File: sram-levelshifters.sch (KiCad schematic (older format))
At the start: 25 parts, among them U10 TXB0108-PW, U11 ISSI61WV5128BL, U12 ISSI61WV5128BL, U13 ISSI61WV5128BL, U14 ISSI61WV5128BL, U4 TXB0108-PW, U5 TXB0108-PW, U6 TXB0108-PW, U7 74HC04, U8 TXB0108-PW, U9 74LS32

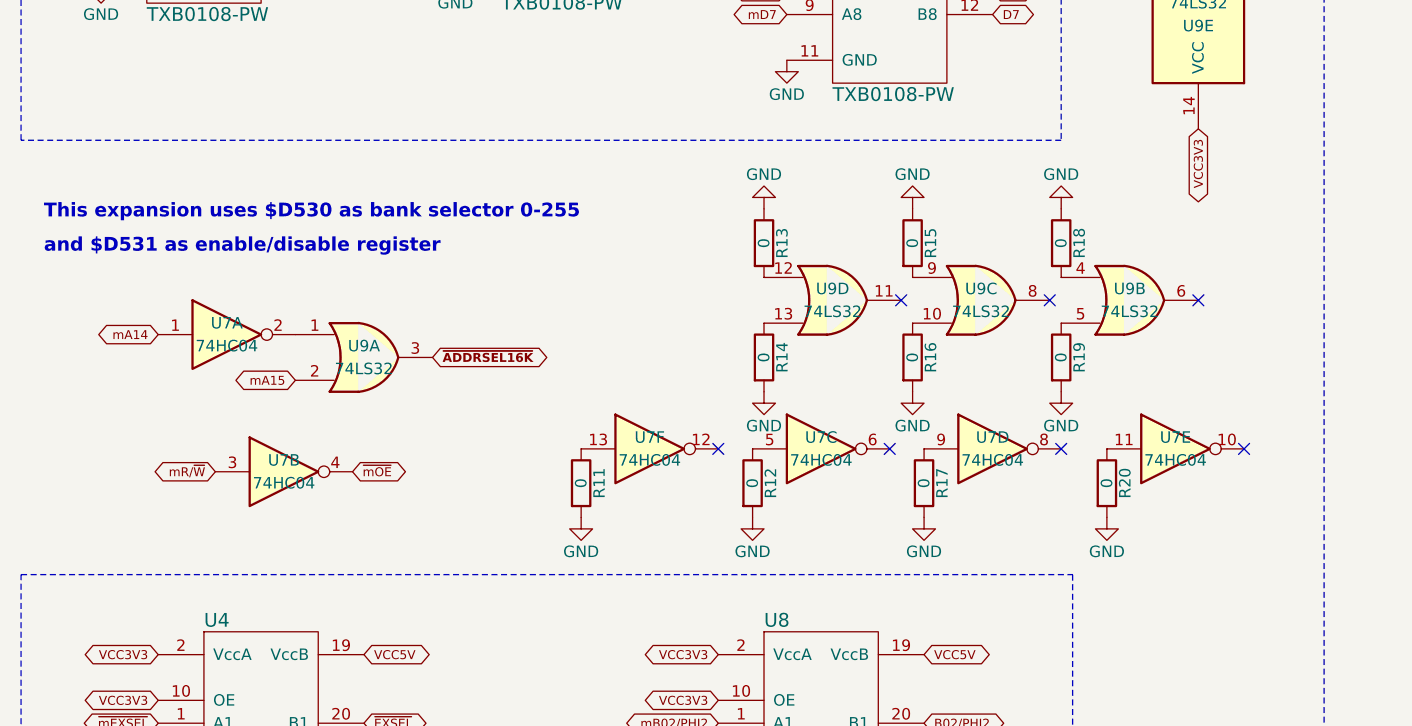
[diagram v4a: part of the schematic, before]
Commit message: Added D3xx selection logic for PIA (6520) if needed
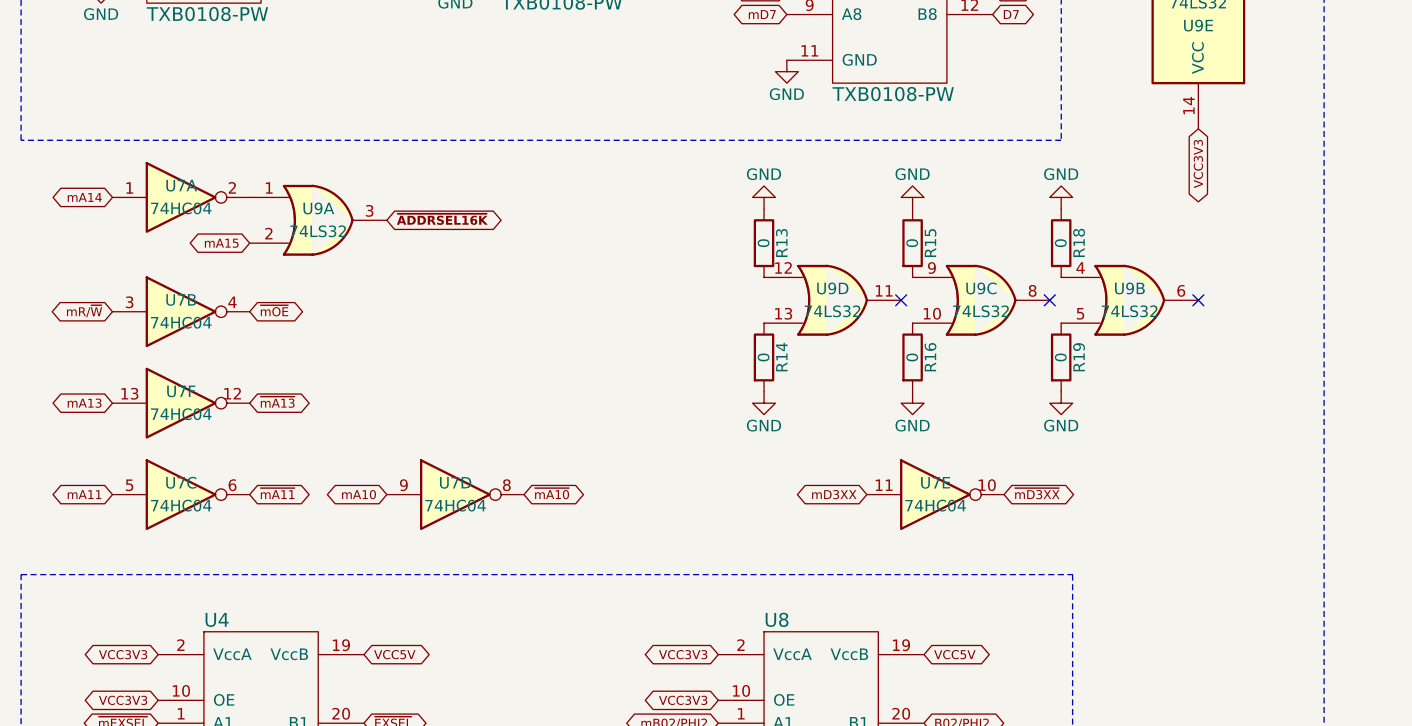
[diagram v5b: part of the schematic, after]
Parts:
- removed R11, R12, R17, R20: 0, Resistors_SMD:R_1206_HandSoldering, symbol R
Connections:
- net mA10: now also U7.9
- net mA11: now also U7.5
- net mA13: now also U7.13
- net ~mA11: now reaches U7.6
- net ~mA10: now reaches U7.8
- net ~mD3XX: now reaches U7.10
- net mD3XX: now reaches U7.11
- net ~mA13: now reaches U7.12
- no-connect marks 11 -> 7
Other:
- note removed: "This expansion uses $D530 as bank selector 0-255"
- note removed: "and $D531 as enable/disable register"
- moved on the sheet: U7A, U7B, U7C, U7D, U7E, U7F, U9A
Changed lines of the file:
@@
 Text Notes 6450 800  0    59   ~ 12
 STATIC RAM
-Text GLabel 2400 3900 2    39   BiDi ~ 8
+Text GLabel 2200 3300 2    39   BiDi ~ 8
 ~ADDRSEL16K
 $Comp
 L 74LS32 U9
 U 1 1 5C2DFACA
-P 2100 3900
-F 0 "U9" H 2100 3950 50  0000 C CNN
-F 1 "74LS32" H 2100 3850 50  0000 C CNN
-F 2 "Housings_SSOP:SSOP-14_5.3x6.2mm_Pitch0.65mm" H 2100 3900 50  0001 C CNN
-F 3 "" H 2100 3900 60  0001 C CNN
-	1    2100 3900
+P 1900 3300
+F 0 "U9" H 1900 3350 50  0000 C CNN
+F 1 "74LS32" H 1900 3250 50  0000 C CNN
+F 2 "Housings_SSOP:SSOP-14_5.3x6.2mm_Pitch0.65mm" H 1900 3300 50  0001 C CNN
+F 3 "" H 1900 3300 60  0001 C CNN
+	1    1900 3300
 	1    0    0    -1
 $EndComp
@@
 NoConn ~ 5100 3650
 NoConn ~ 4450 3650
-Text GLabel 1800 4000 0    39   BiDi ~ 0
+Text GLabel 1600 3400 0    39   BiDi ~ 0
 mA15
-Text GLabel 1200 3800 0    39   BiDi ~ 0
+Text GLabel 1000 3200 0    39   BiDi ~ 0
 mA14
 $Comp
 L 74HC04 U7
 U 1 1 5C2DFE46
-P 1500 3800
-F 0 "U7" H 1500 3850 50  0000 C CNN
-F 1 "74HC04" H 1500 3750 50  0000 C CNN
-F 2 "Housings_SSOP:TSSOP-14_4.4x5mm_Pitch0.65mm" H 1500 3800 50  0001 C CNN
-F 3 "" H 1500 3800 60  0001 C CNN
-	1    1500 3800
+P 1300 3200
+F 0 "U7" H 1300 3250 50  0000 C CNN
+F 1 "74HC04" H 1300 3150 50  0000 C CNN
+F 2 "Housings_SSOP:TSSOP-14_4.4x5mm_Pitch0.65mm" H 1300 3200 50  0001 C CNN
+F 3 "" H 1300 3200 60  0001 C CNN
+	1    1300 3200
 	1    0    0    -1
 $EndComp
@@
 L 74HC04 U7
 U 2 1 5C2DFEE1
-P 1750 4400
-F 0 "U7" H 1750 4450 50  0000 C CNN
-F 1 "74HC04" H 1750 4350 50  0000 C CNN
-F 2 "Housings_SSOP:TSSOP-14_4.4x5mm_Pitch0.65mm" H 1750 4400 50  0001 C CNN
-F 3 "" H 1750 4400 60  0001 C CNN
-	2    1750 4400
+P 1300 3700
+F 0 "U7" H 1300 3750 50  0000 C CNN
+F 1 "74HC04" H 1300 3650 50  0000 C CNN
+F 2 "Housings_SSOP:TSSOP-14_4.4x5mm_Pitch0.65mm" H 1300 3700 50  0001 C CNN
+F 3 "" H 1300 3700 60  0001 C CNN
+	2    1300 3700
 	1    0    0    -1
 $EndComp
@@
 L 74HC04 U7
 U 3 1 5C2DFF28
-P 4100 4300
-F 0 "U7" H 4100 4350 50  0000 C CNN
-F 1 "74HC04" H 4100 4250 50  0000 C CNN
-F 2 "Housings_SSOP:TSSOP-14_4.4x5mm_Pitch0.65mm" H 4100 4300 50  0001 C CNN
-F 3 "" H 4100 4300 60  0001 C CNN
-	3    4100 4300
+P 1300 4500
+F 0 "U7" H 1300 4550 50  0000 C CNN
+F 1 "74HC04" H 1300 4450 50  0000 C CNN
+F 2 "Housings_SSOP:TSSOP-14_4.4x5mm_Pitch0.65mm" H 1300 4500 50  0001 C CNN
+F 3 "" H 1300 4500 60  0001 C CNN
+	3    1300 4500
 	1    0    0    -1
 $EndComp
@@
 L 74HC04 U7
 U 4 1 5C2E0001
-P 4850 4300
-F 0 "U7" H 4850 4350 50  0000 C CNN
-F 1 "74HC04" H 4850 4250 50  0000 C CNN
-F 2 "Housings_SSOP:TSSOP-14_4.4x5mm_Pitch0.65mm" H 4850 4300 50  0001 C CNN
-F 3 "" H 4850 4300 60  0001 C CNN
-	4    4850 4300
+P 2500 4500
+F 0 "U7" H 2500 4550 50  0000 C CNN
+F 1 "74HC04" H 2500 4450 50  0000 C CNN
+F 2 "Housings_SSOP:TSSOP-14_4.4x5mm_Pitch0.65mm" H 2500 4500 50  0001 C CNN
+F 3 "" H 2500 4500 60  0001 C CNN
+	4    2500 4500
 	1    0    0    -1
 $EndComp
@@
 L 74HC04 U7
 U 5 1 5C2E0114
-P 5650 4300
-F 0 "U7" H 5650 4350 50  0000 C CNN
-F 1 "74HC04" H 5650 4250 50  0000 C CNN
-F 2 "Housings_SSOP:TSSOP-14_4.4x5mm_Pitch0.65mm" H 5650 4300 50  0001 C CNN
-F 3 "" H 5650 4300 60  0001 C CNN
-	5    5650 4300
+P 4600 4500
+F 0 "U7" H 4600 4550 50  0000 C CNN
+F 1 "74HC04" H 4600 4450 50  0000 C CNN
+F 2 "Housings_SSOP:TSSOP-14_4.4x5mm_Pitch0.65mm" H 4600 4500 50  0001 C CNN
+F 3 "" H 4600 4500 60  0001 C CNN
+	5    4600 4500
 	1    0    0    -1
 $EndComp
@@
 L 74HC04 U7
 U 6 1 5C2E0161
-P 3350 4300
-F 0 "U7" H 3350 4350 50  0000 C CNN
-F 1 "74HC04" H 3350 4250 50  0000 C CNN
-F 2 "Housings_SSOP:TSSOP-14_4.4x5mm_Pitch0.65mm" H 3350 4300 50  0001 C CNN
-F 3 "" H 3350 4300 60  0001 C CNN
-	6    3350 4300
+P 1300 4100
+F 0 "U7" H 1300 4150 50  0000 C CNN
+F 1 "74HC04" H 1300 4050 50  0000 C CNN
+F 2 "Housings_SSOP:TSSOP-14_4.4x5mm_Pitch0.65mm" H 1300 4100 50  0001 C CNN
+F 3 "" H 1300 4100 60  0001 C CNN
+	6    1300 4100
 	1    0    0    -1
 $EndComp
@@
 Text GLabel 7150 6050 0    39   BiDi ~ 0
 PB4
-Text GLabel 1450 4400 0    39   BiDi ~ 0
+Text GLabel 1000 3700 0    39   BiDi ~ 0
 mR/~W
-Text GLabel 2050 4400 2    39   BiDi ~ 0
+Text GLabel 1600 3700 2    39   BiDi ~ 0
 ~mOE
 Text GLabel 8350 2650 3    39   BiDi ~ 0
@@
 Text GLabel 8350 5550 3    39   BiDi ~ 0
 ~mOE
-Text Notes 700  3300 0    60   ~ 12
-This expansion uses $D530 as bank selector 0-255
-Text Notes 700  3450 0    60   ~ 12
-and $D531 as enable/disable register
 Text GLabel 4550 5700 2    39   BiDi ~ 0
 ~S4
@@
 Text GLabel 3650 5700 0    39   BiDi ~ 0
 ~mS4
-NoConn ~ 3650 4300
-NoConn ~ 4400 4300
-NoConn ~ 5150 4300
-NoConn ~ 5950 4300
-$Comp
-L GND #PWR041
-U 1 1 5C371152
-P 5350 4600
-F 0 "#PWR041" H 5350 4350 50  0001 C CNN
-F 1 "GND" H 5350 4450 50  0000 C CNN
-F 2 "" H 5350 4600 50  0001 C CNN
-F 3 "" H 5350 4600 50  0001 C CNN
-	1    5350 4600
-	1    0    0    -1
-$EndComp
-$Comp
-L R R20
-U 1 1 5C371196
-P 5350 4450
-F 0 "R20" V 5430 4450 50  0000 C CNN
-F 1 "0" V 5350 4450 50  0000 C CNN
-F 2 "Resistors_SMD:R_1206_HandSoldering" V 5280 4450 50  0001 C CNN
-F 3 "" H 5350 4450 50  0000 C CNN
-	1    5350 4450
-	1    0    0    -1
-$EndComp
-$Comp
-L R R17
-U 1 1 5C37121E
-P 4550 4450
-F 0 "R17" V 4630 4450 50  0000 C CNN
-F 1 "0" V 4550 4450 50  0000 C CNN
-F 2 "Resistors_SMD:R_1206_HandSoldering" V 4480 4450 50  0001 C CNN
-F 3 "" H 4550 4450 50  0000 C CNN
-	1    4550 4450
-	1    0    0    -1
-$EndComp
-$Comp
-L R R12
-U 1 1 5C371304
-P 3800 4450
-F 0 "R12" V 3880 4450 50  0000 C CNN
-F 1 "0" V 3800 4450 50  0000 C CNN
-F 2 "Resistors_SMD:R_1206_HandSoldering" V 3730 4450 50  0001 C CNN
-F 3 "" H 3800 4450 50  0000 C CNN
-	1    3800 4450
-	1    0    0    -1
-$EndComp
-$Comp
-L R R11
-U 1 1 5C3713A0
-P 3050 4450
-F 0 "R11" V 3130 4450 50  0000 C CNN
-F 1 "0" V 3050 4450 50  0000 C CNN
-F 2 "Resistors_SMD:R_1206_HandSoldering" V 2980 4450 50  0001 C CNN
-F 3 "" H 3050 4450 50  0000 C CNN
-	1    3050 4450
-	1    0    0    -1
-$EndComp
-$Comp
-L GND #PWR042
-U 1 1 5C37141A
-P 4550 4600
-F 0 "#PWR042" H 4550 4350 50  0001 C CNN
-F 1 "GND" H 4550 4450 50  0000 C CNN
-F 2 "" H 4550 4600 50  0001 C CNN
-F 3 "" H 4550 4600 50  0001 C CNN
-	1    4550 4600
-	1    0    0    -1
-$EndComp
-$Comp
-L GND #PWR043
-U 1 1 5C371479
-P 3800 4600
-F 0 "#PWR043" H 3800 4350 50  0001 C CNN
-F 1 "GND" H 3800 4450 50  0000 C CNN
-F 2 "" H 3800 4600 50  0001 C CNN
-F 3 "" H 3800 4600 50  0001 C CNN
-	1    3800 4600
-	1    0    0    -1
-$EndComp
-$Comp
-L GND #PWR044
-U 1 1 5C3714D8
-P 3050 4600
-F 0 "#PWR044" H 3050 4350 50  0001 C CNN
-F 1 "GND" H 3050 4450 50  0000 C CNN
-F 2 "" H 3050 4600 50  0001 C CNN
-F 3 "" H 3050 4600 50  0001 C CNN
-	1    3050 4600
-	1    0    0    -1
-$EndComp
 $Comp
 L R R14
@@
 $EndComp
 $Comp
-L GND #PWR045
+L GND #PWR041
 U 1 1 5C371981
 P 5150 3250
-F 0 "#PWR045" H 5150 3000 50  0001 C CNN
+F 0 "#PWR041" H 5150 3000 50  0001 C CNN
 F 1 "GND" H 5150 3100 50  0000 C CNN
 F 2 "" H 5150 3250 50  0001 C CNN
@@
 $EndComp
 $Comp
-L GND #PWR046
+L GND #PWR042
 U 1 1 5C3719F2
 P 4500 3250
-F 0 "#PWR046" H 4500 3000 50  0001 C CNN
+F 0 "#PWR042" H 4500 3000 50  0001 C CNN
 F 1 "GND" H 4500 3100 50  0000 C CNN
 F 2 "" H 4500 3250 50  0001 C CNN
@@
 $EndComp
 $Comp
-L GND #PWR047
+L GND #PWR043
 U 1 1 5C371A63
 P 3850 3250
-F 0 "#PWR047" H 3850 3000 50  0001 C CNN
+F 0 "#PWR043" H 3850 3000 50  0001 C CNN
 F 1 "GND" H 3850 3100 50  0000 C CNN
 F 2 "" H 3850 3250 50  0001 C CNN
@@
 $EndComp
 $Comp
-L GND #PWR048
+L GND #PWR044
 U 1 1 5C371AD4
 P 3850 4050
-F 0 "#PWR048" H 3850 3800 50  0001 C CNN
+F 0 "#PWR044" H 3850 3800 50  0001 C CNN
 F 1 "GND" H 3850 3900 50  0000 C CNN
 F 2 "" H 3850 4050 50  0001 C CNN
@@
 $EndComp
 $Comp
-L GND #PWR049
+L GND #PWR045
 U 1 1 5C371B45
 P 4500 4050
-F 0 "#PWR049" H 4500 3800 50  0001 C CNN
+F 0 "#PWR045" H 4500 3800 50  0001 C CNN
 F 1 "GND" H 4500 3900 50  0000 C CNN
 F 2 "" H 4500 4050 50  0001 C CNN
@@
 $EndComp
 $Comp
-L GND #PWR050
+L GND #PWR046
 U 1 1 5C371BB6
 P 5150 4050
-F 0 "#PWR050" H 5150 3800 50  0001 C CNN
+F 0 "#PWR046" H 5150 3800 50  0001 C CNN
 F 1 "GND" H 5150 3900 50  0000 C CNN
 F 2 "" H 5150 4050 50  0001 C CNN
@@
 VCC5V
 $Comp
-L GND #PWR051
+L GND #PWR047
 U 1 1 5C374058
 P 2500 2200
-F 0 "#PWR051" H 2500 1950 50  0001 C CNN
+F 0 "#PWR047" H 2500 1950 50  0001 C CNN
 F 1 "GND" H 2500 2050 50  0000 C CNN
 F 2 "" H 2500 2200 60  0001 C CNN
@@
 NoConn ~ 3650 6200
 NoConn ~ 3650 6100
+Text GLabel 1000 4100 0    39   BiDi ~ 0
+mA13
+Text GLabel 1600 4100 2    39   BiDi ~ 0
+~mA13
+Text GLabel 1000 4500 0    39   BiDi ~ 0
+mA11
+Text GLabel 1600 4500 2    39   BiDi ~ 0
+~mA11
+Text GLabel 2200 4500 0    39   BiDi ~ 0
+mA10
+Text GLabel 2800 4500 2    39   BiDi ~ 0
+~mA10
+Text GLabel 4300 4500 0    39   BiDi ~ 0
+mD3XX
+Text GLabel 4900 4500 2    39   BiDi ~ 0
+~mD3XX
 $EndSCHEMATC

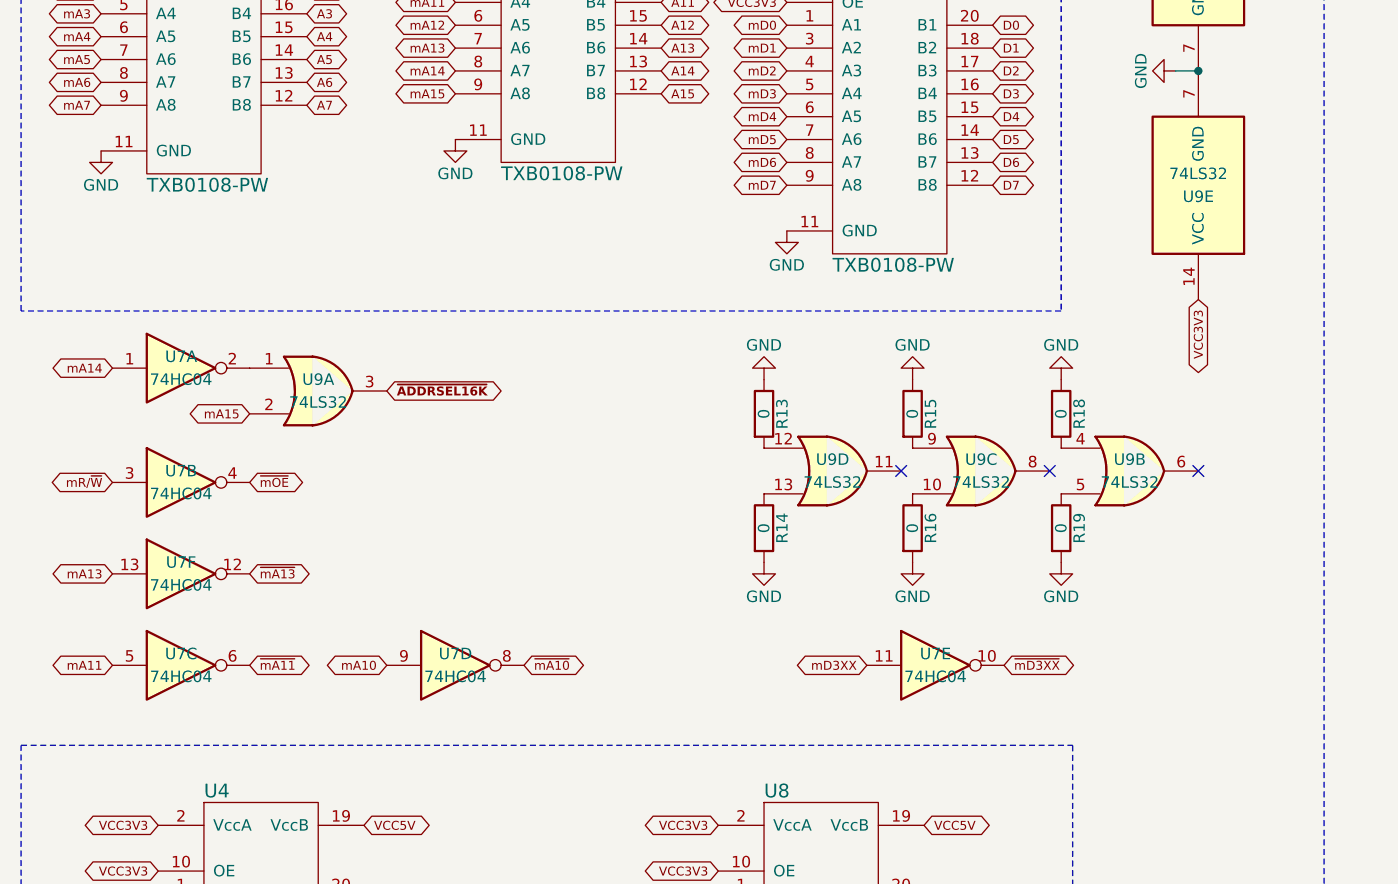
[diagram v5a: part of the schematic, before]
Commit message: Modified for new MCU
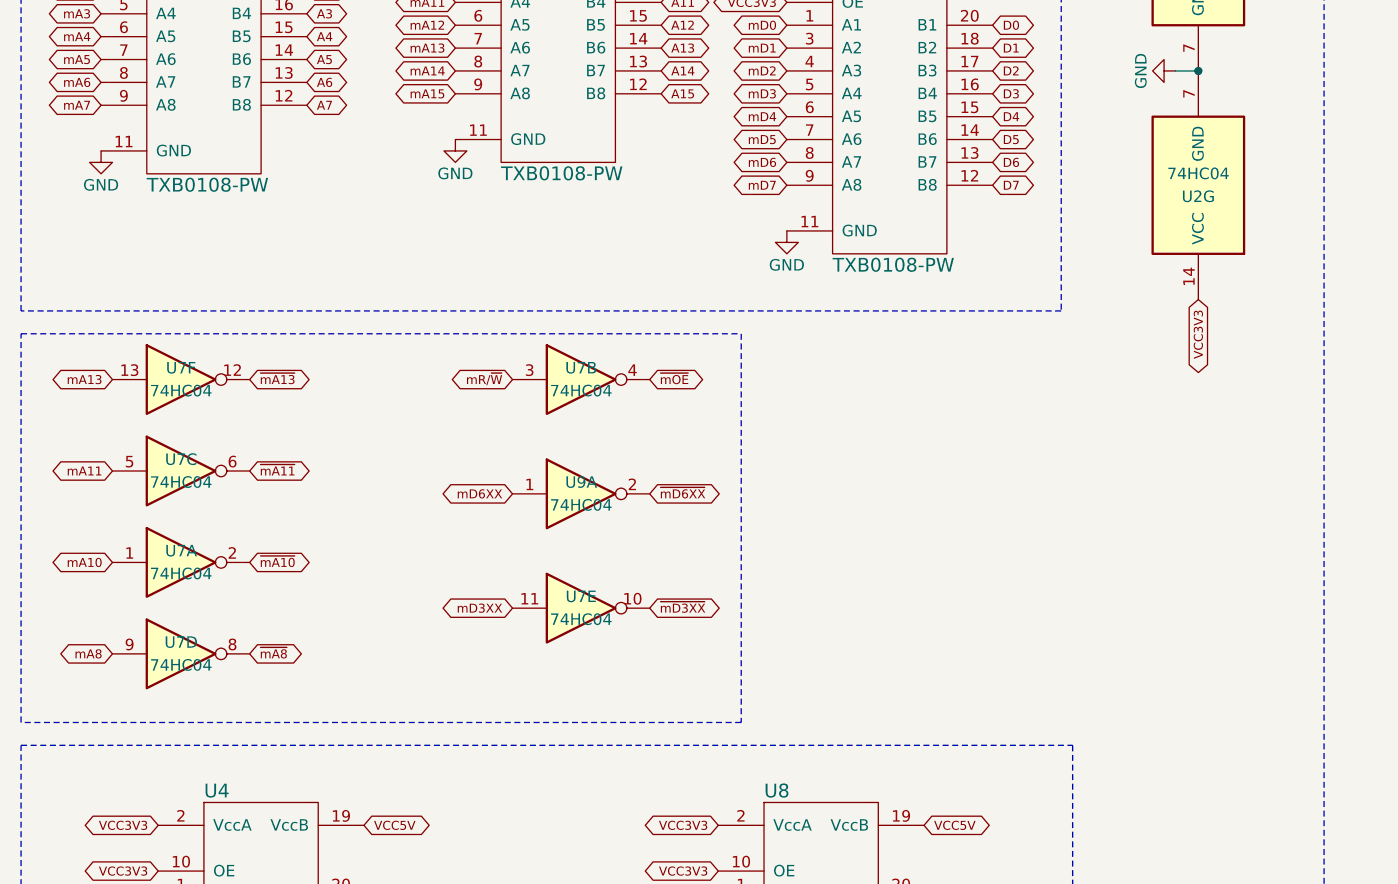
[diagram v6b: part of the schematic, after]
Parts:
- removed R13, R14, R15, R16, R18, R19: 0, Resistors_SMD:R_1206_HandSoldering, symbol R
- removed U9: 74LS32, Housings_SSOP:SSOP-14_5.3x6.2mm_Pitch0.65mm, symbol 74LS32
- added U2, U9: 74HC04, Housings_SSOP:TSSOP-14_4.4x5mm_Pitch0.65mm, symbol 74HC04
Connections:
- net GND: now also U2.7 (GND)
- net VCC3V3: now also U2.14 (VCC)
- net mA10: now also U7.1; no longer U7.9
- net mA14: no longer U7.1
- net mA8: now also U7.9
- net ~mA10: now also U7.2; no longer U7.8
- new net mD6XX: U9.1
- new net ~mA8: U7.8
- new net ~mD6XX: U9.2
- no-connect marks 7 -> 4
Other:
- moved on the sheet: U7A, U7B, U7C, U7D, U7E, U7F

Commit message: Transformation will begin shortly... ;-)
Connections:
- net mA10: no longer U11.23 (A10), U12.23 (A10), U13.23 (A10), U14.23 (A10)
- net mA11: no longer U11.25 (A11), U12.25 (A11), U13.25 (A11), U14.25 (A11)
- net mA12: no longer U11.4 (A12), U12.4 (A12), U13.4 (A12), U14.4 (A12)
- net mA13: no longer U11.28 (A13), U12.28 (A13), U13.28 (A13), U14.28 (A13)
- net mA8: no longer U11.27 (A8), U12.27 (A8), U13.27 (A8), U14.27 (A8)
- net mA9: no longer U11.26 (A9), U12.26 (A9), U13.26 (A9), U14.26 (A9)
- net PB0 renamed mD1E0_A14
- net PB1 renamed mD1E0_A15
- net PB2 renamed mD1E2_A16
- net PB3 renamed mD1E2_A17
- net PB4 renamed mD1E2_A18
- new net mD1E0_A10: U11.23 (A10), U12.23 (A10), U13.23 (A10), U14.23 (A10)
- new net mD1E0_A11: U11.25 (A11), U12.25 (A11), U13.25 (A11), U14.25 (A11)
- new net mD1E0_A12: U11.4 (A12), U12.4 (A12), U13.4 (A12), U14.4 (A12)
- new net mD1E0_A13: U11.28 (A13), U12.28 (A13), U13.28 (A13), U14.28 (A13)
- new net mD1E0_A8: U11.27 (A8), U12.27 (A8), U13.27 (A8), U14.27 (A8)
- new net mD1E0_A9: U11.26 (A9), U12.26 (A9), U13.26 (A9), U14.26 (A9)
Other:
- moved on the sheet: U10, U2G, U7G
